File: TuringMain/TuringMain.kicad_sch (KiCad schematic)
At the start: 108 parts, among them IC1 TL072P, IC2 78L09, IC3 78L09, J1 Conn_01x10_Male, J2 Conn_01x10_Female, T1 2N3904, U1 TL074_

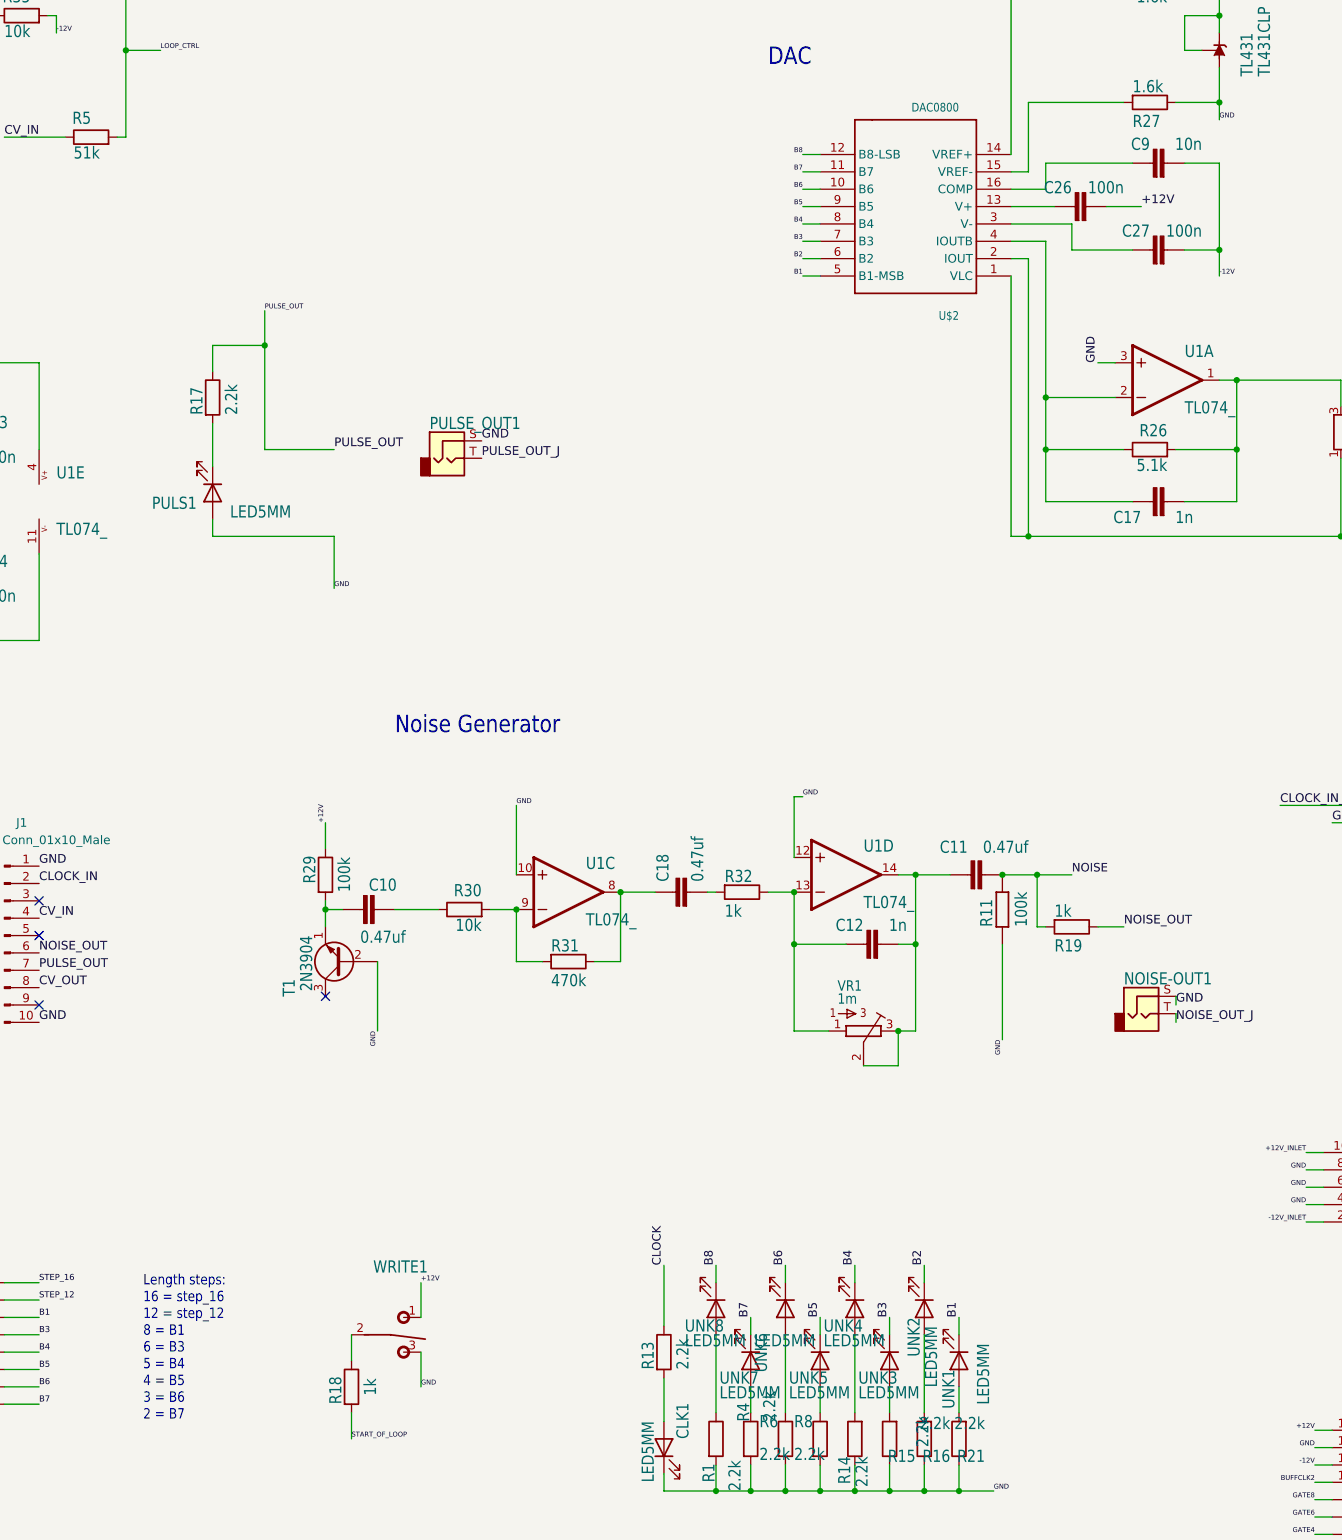
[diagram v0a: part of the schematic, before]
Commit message: Manufacturing Updates
Rotary Switch Panel Drill Corrected
Panel Graphics Changed (Name changed from Turing Machine to The Halting Problem)
Updated silkscreen on mainboard with circuit corrections and component values.
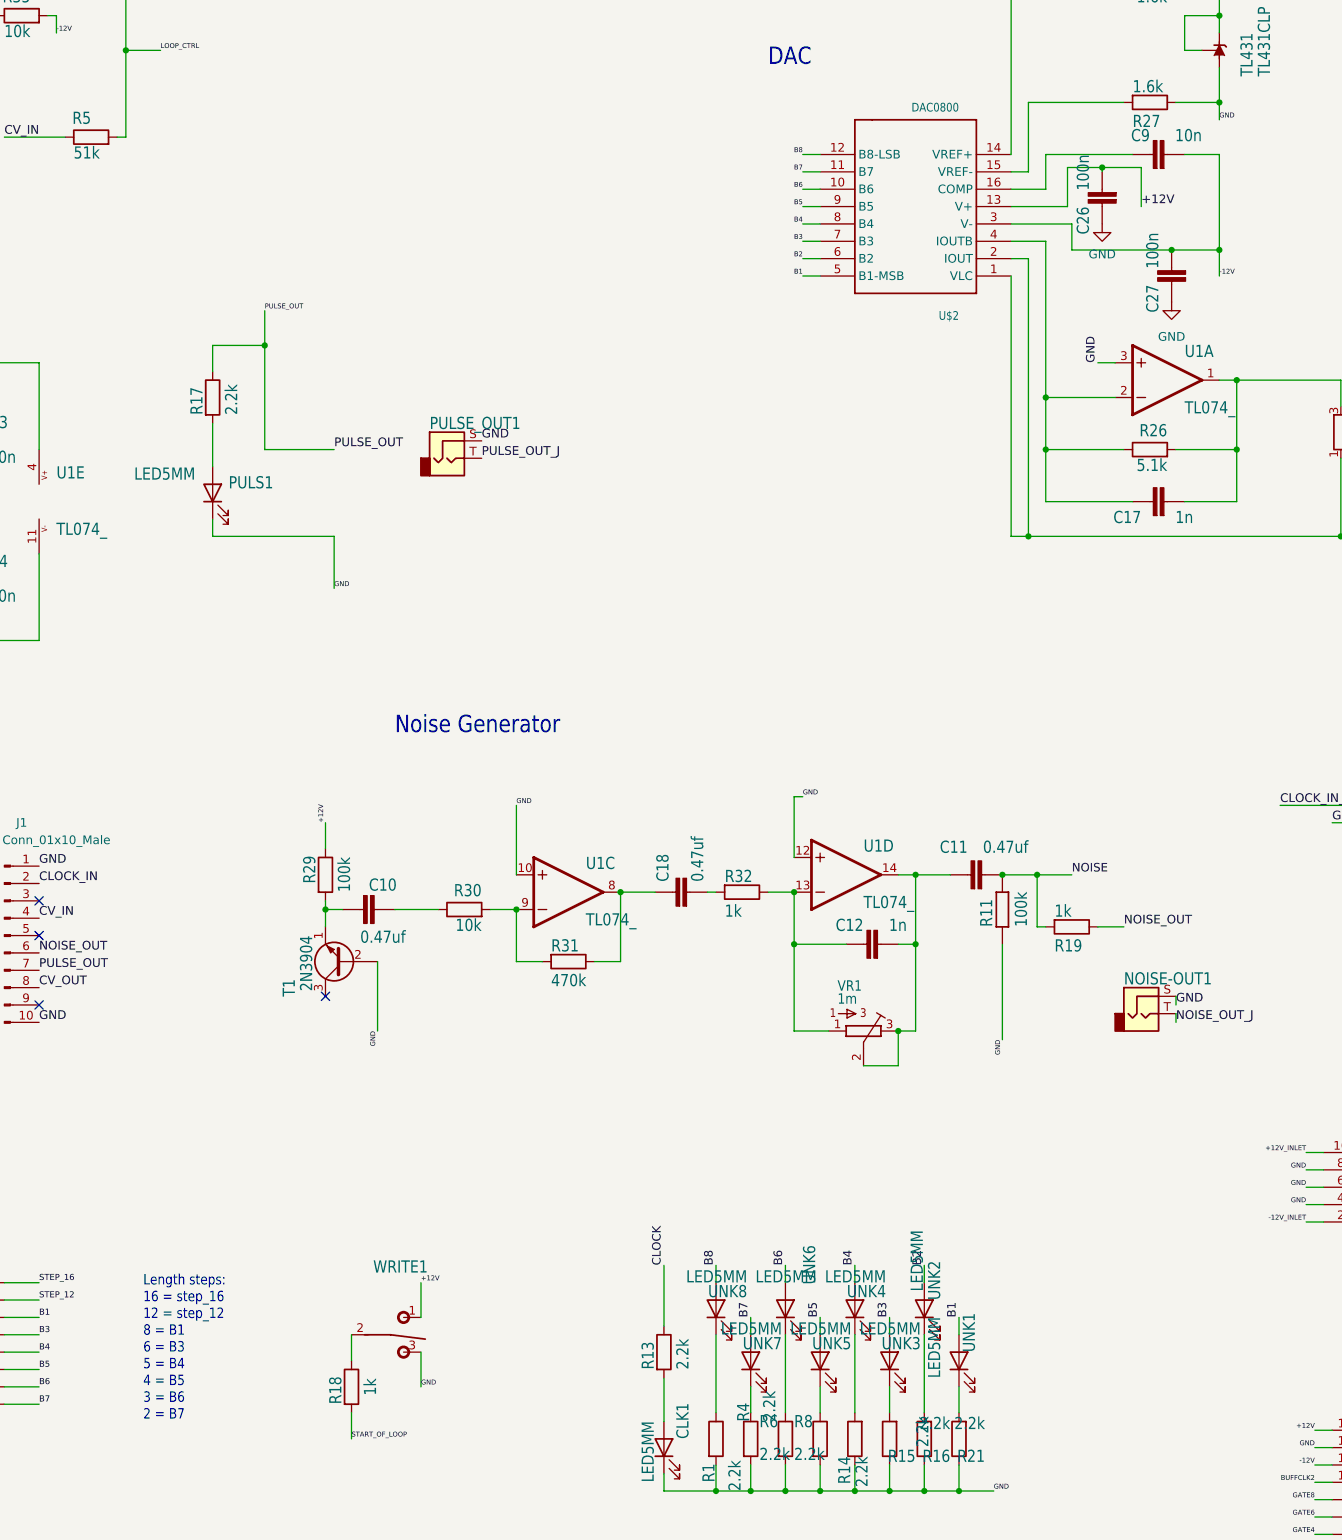
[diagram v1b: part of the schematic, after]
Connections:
- net +12V: now also U$2.13 (V+)
- net -12V: now also U$2.3 (V-)
- net B1: now also UNK1.2 (A); no longer UNK1.1 (K)
- net B2: now also UNK2.2 (A); no longer UNK2.1 (K)
- net B3: now also UNK3.2 (A); no longer UNK3.1 (K)
- net B4: now also UNK4.2 (A); no longer UNK4.1 (K)
- net B5: now also UNK5.2 (A); no longer UNK5.1 (K)
- net B6: now also UNK6.2 (A); no longer UNK6.1 (K)
- net B7: now also UNK7.2 (A); no longer UNK7.1 (K)
- net B8: now also UNK8.2 (A); no longer UNK8.1 (K)
- net GND: now also C26.1, C27.1, PULS1.1 (K); no longer PULS1.2 (A)
- net at R4.1: now also UNK7.1 (K); no longer UNK7.2 (A)
- net at R15.2: now also UNK3.1 (K); no longer UNK3.2 (A)
- net at R6.1: now also UNK6.1 (K); no longer UNK6.2 (A)
- net at R16.2: now also UNK2.1 (K); no longer UNK2.2 (A)
- net at R17.2: now also PULS1.2 (A); no longer PULS1.1 (K)
- net at R14.2: now also UNK4.1 (K); no longer UNK4.2 (A)
- net at R21.2: now also UNK1.1 (K); no longer UNK1.2 (A)
- net at R8.1: now also UNK5.1 (K); no longer UNK5.2 (A)
- net at R1.1: now also UNK8.1 (K); no longer UNK8.2 (A)
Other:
- moved on the sheet: C26, C27, C9, PULS1, UNK1, UNK2, UNK3, UNK4, UNK5, UNK6, UNK7, UNK8

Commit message: Minor Main Board updates
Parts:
- IC2, IC3, TL431: footprint Package_TO_SOT_THT:TO-92_Inline -> ao_tht:TO-92_Inline_Wide
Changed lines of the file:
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@@
   (symbol (lib_id "TuringBack-eagle-import:4016N") (at 494.03 100.33 0) (unit 4)
     (in_bom yes) (on_board yes)
-    (property "Reference" "SWITCH_IC1" (id 0) (at 486.41 109.22 0)
+    (property "Reference" "SWITCH_IC1" (id 0) (at 486.41 109.855 0)
       (effects (font (size 1.778 1.5113)) (justify left bottom))
     )
-    (property "Value" "4016" (id 1) (at 486.41 107.95 0)
+    (property "Value" "4016" (id 1) (at 491.49 101.6 0)
       (effects (font (size 1.778 1.5113)) (justify left bottom))
     )
@@
       (effects (font (size 1.778 1.5113)) (justify left bottom))
     )
-    (property "Footprint" "Package_TO_SOT_THT:TO-92_Inline" (id 2) (at 590.55 126.365 0)
+    (property "Footprint" "ao_tht:TO-92_Inline_Wide" (id 2) (at 590.55 126.365 0)
       (effects (font (size 1.27 1.27) italic) hide)
     )
@@
       (effects (font (size 1.778 1.5113)) (justify left bottom))
     )
-    (property "Footprint" "Package_TO_SOT_THT:TO-92_Inline" (id 2) (at 565.15 126.365 0)
+    (property "Footprint" "ao_tht:TO-92_Inline_Wide" (id 2) (at 565.15 126.365 0)
       (effects (font (size 1.27 1.27) italic) hide)
     )
@@
   (symbol (lib_id "ao_symbols:LED_green") (at 205.74 252.73 90) (unit 1)
     (in_bom yes) (on_board yes)
-    (property "Reference" "UNK3" (id 0) (at 210.312 249.174 90)
+    (property "Reference" "UNK3" (id 0) (at 208.28 248.92 0)
       (effects (font (size 1.778 1.5113)) (justify left bottom))
     )
-    (property "Value" "LED5MM" (id 1) (at 210.312 247.015 90)
+    (property "Value" "LED5MM" (id 1) (at 210.82 248.92 0)
       (effects (font (size 1.778 1.5113)) (justify left bottom))
     )
@@
   (symbol (lib_id "ao_symbols:LED_green") (at 210.82 245.11 90) (unit 1)
     (in_bom yes) (on_board yes)
-    (property "Reference" "UNK2" (id 0) (at 213.36 243.84 0)
+    (property "Reference" "UNK2" (id 0) (at 214.63 243.205 0)
       (effects (font (size 1.778 1.5113)) (justify left bottom))
     )
-    (property "Value" "LED5MM" (id 1) (at 210.82 242.57 0)
+    (property "Value" "LED5MM" (id 1) (at 217.17 243.205 0)
       (effects (font (size 1.778 1.5113)) (justify left bottom))
     )
@@
       (effects (font (size 1.778 1.5113)) (justify left bottom))
     )
-    (property "Footprint" "Package_TO_SOT_THT:TO-92_Inline" (id 2) (at 257.81 60.96 0)
+    (property "Footprint" "ao_tht:TO-92_Inline_Wide" (id 2) (at 257.81 60.96 0)
       (effects (font (size 1.27 1.27) italic) hide)
     )
@@
   (symbol (lib_id "ao_symbols:LED_green") (at 190.5 245.11 90) (unit 1)
     (in_bom yes) (on_board yes)
-    (property "Reference" "UNK6" (id 0) (at 195.072 241.554 0)
+    (property "Reference" "UNK6" (id 0) (at 194.31 240.665 0)
       (effects (font (size 1.778 1.5113)) (justify left bottom))
     )
@@
   (symbol (lib_id "ao_symbols:LED_green") (at 215.9 252.73 90) (unit 1)
     (in_bom yes) (on_board yes)
-    (property "Reference" "UNK1" (id 0) (at 218.44 251.46 0)
+    (property "Reference" "UNK1" (id 0) (at 221.615 255.905 0)
       (effects (font (size 1.778 1.5113)) (justify left bottom))
     )
-    (property "Value" "LED5MM" (id 1) (at 213.36 255.27 0)
+    (property "Value" "LED5MM" (id 1) (at 224.79 255.905 0)
       (effects (font (size 1.778 1.5113)) (justify left bottom))
     )
@@
   (symbol (lib_id "TuringBack-eagle-import:4081N") (at 515.62 257.81 0) (unit 1)
     (in_bom yes) (on_board yes)
-    (property "Reference" "AND_2" (id 0) (at 514.35 258.445 0)
+    (property "Reference" "AND_2" (id 0) (at 516.89 266.7 0)
       (effects (font (size 1.778 1.5113)) (justify left bottom))
     )
@@
       (effects (font (size 1.778 1.5113)) (justify left bottom))
     )
-    (property "Value" "4016" (id 1) (at 519.43 36.83 0)
+    (property "Value" "4016" (id 1) (at 523.875 31.115 0)
       (effects (font (size 1.778 1.5113)) (justify left bottom))
     )
@@
       (effects (font (size 1.778 1.5113)) (justify left bottom))
     )
-    (property "Value" "4015" (id 1) (at 664.21 125.73 0)
+    (property "Value" "4015" (id 1) (at 662.94 121.285 0)
       (effects (font (size 1.778 1.5113)) (justify left bottom))
     )
@@
   (symbol (lib_id "ao_symbols:LED_green") (at 185.42 252.73 90) (unit 1)
     (in_bom yes) (on_board yes)
-    (property "Reference" "UNK7" (id 0) (at 189.992 249.174 90)
+    (property "Reference" "UNK7" (id 0) (at 188.595 250.19 90)
       (effects (font (size 1.778 1.5113)) (justify left bottom))
     )
@@
   (symbol (lib_id "ao_symbols:LED_green") (at 180.34 245.11 90) (unit 1)
     (in_bom yes) (on_board yes)
-    (property "Reference" "UNK8" (id 0) (at 184.912 241.554 90)
+    (property "Reference" "UNK8" (id 0) (at 184.15 242.57 90)
       (effects (font (size 1.778 1.5113)) (justify left bottom))
     )
@@
     )
     (path "/567ac6aa-278e-4592-b80e-f5cd81047e50"
-      (reference "IC2") (unit 1) (value "78L09") (footprint "Package_TO_SOT_THT:TO-92_Inline")
+      (reference "IC2") (unit 1) (value "78L09") (footprint "ao_tht:TO-92_Inline_Wide")
     )
     (path "/29b583c7-0f35-4b9e-9c83-f08988b7fdeb"
-      (reference "IC3") (unit 1) (value "78L09") (footprint "Package_TO_SOT_THT:TO-92_Inline")
+      (reference "IC3") (unit 1) (value "78L09") (footprint "ao_tht:TO-92_Inline_Wide")
     )
     (path "/0394c918-5756-4d55-bbcb-f24d377c8d49"
@@
     )
     (path "/88d667a7-822d-4255-9f05-e05719238808"
-      (reference "TL431") (unit 1) (value "TL431CLP") (footprint "Package_TO_SOT_THT:TO-92_Inline")
+      (reference "TL431") (unit 1) (value "TL431CLP") (footprint "ao_tht:TO-92_Inline_Wide")
     )
     (path "/117b2dd3-5681-4de4-bc26-dffa8c801a74"
